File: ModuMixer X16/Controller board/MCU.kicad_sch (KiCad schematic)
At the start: 2 parts, among them U12 STM32F103RCTx

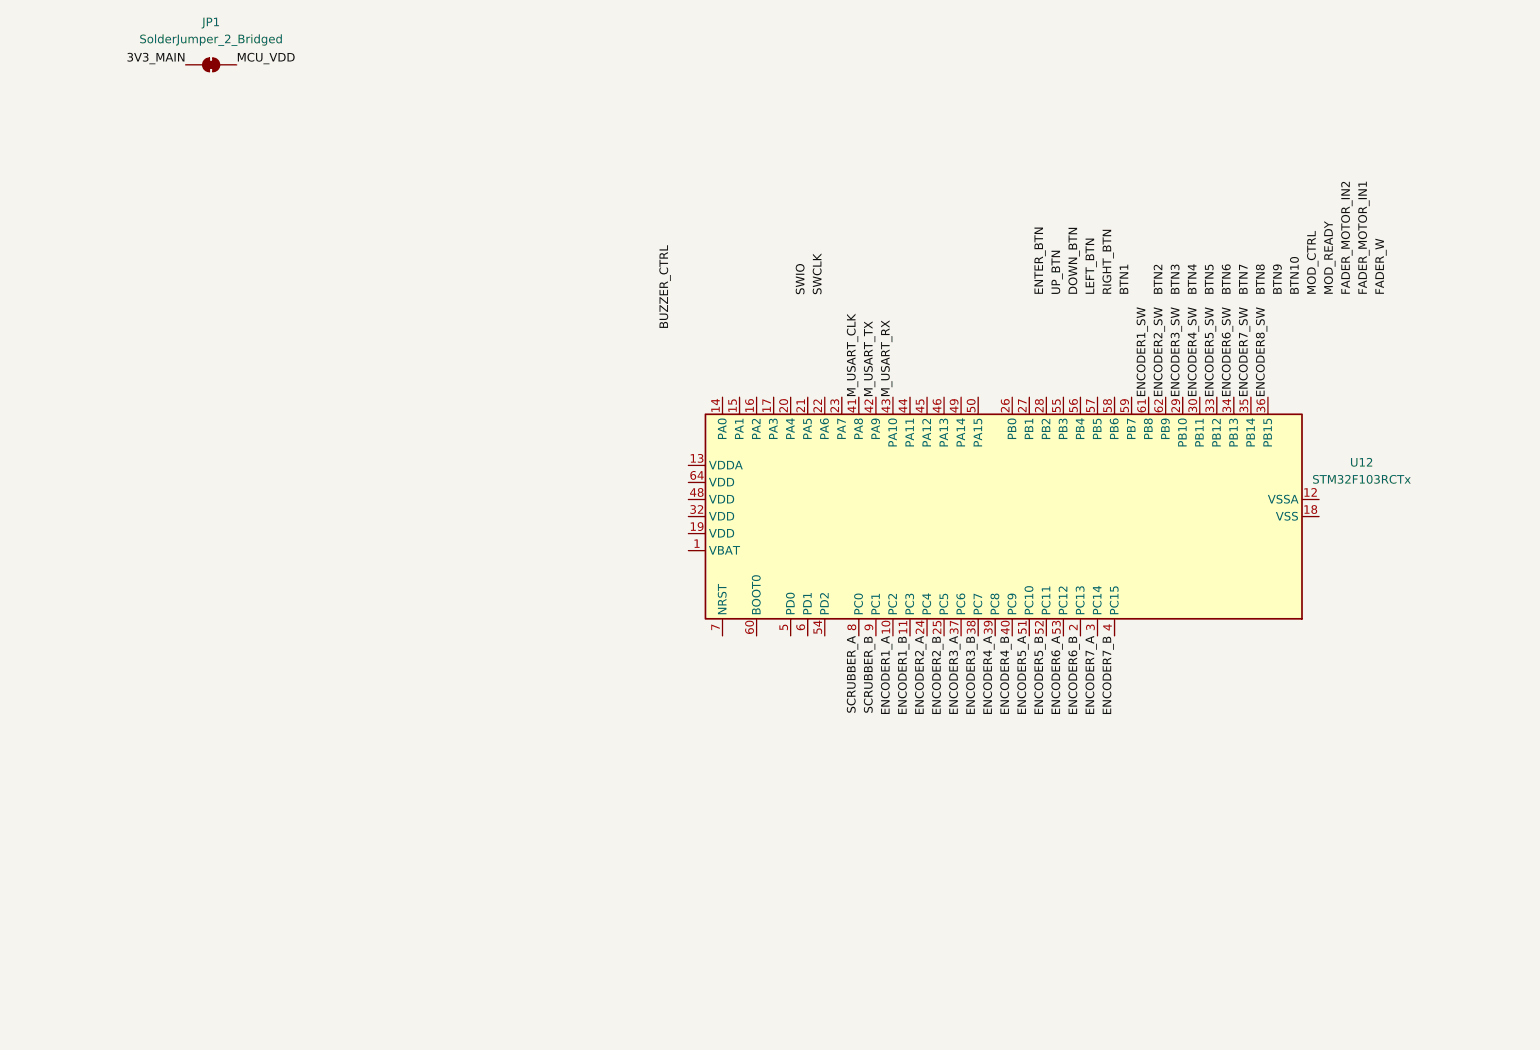
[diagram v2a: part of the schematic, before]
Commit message: Midway through MCU replacement
Sometimes i feel like it would be better to start over considering it's a digital mixer.
The only thing left is doing the DSP connections and calculating the values for a 16mhz crystal on all 3 MCUs
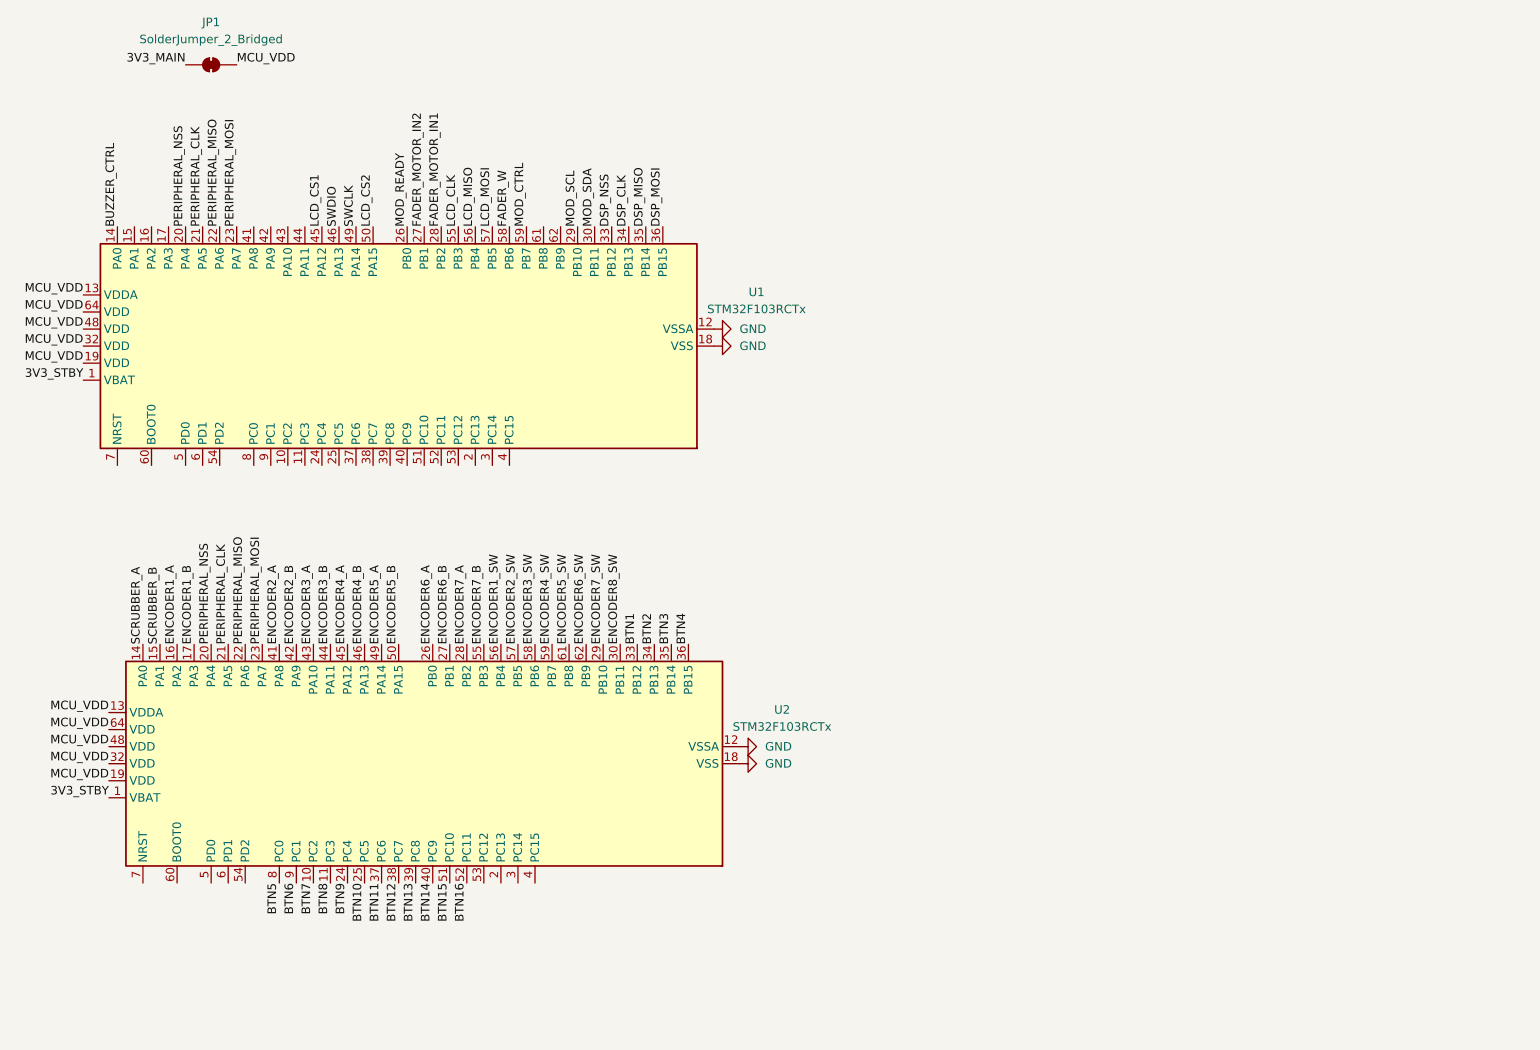
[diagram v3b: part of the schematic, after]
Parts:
- added U2: STM32F103RCTx, Package_QFP:LQFP-64_10x10mm_P0.5mm, symbol MCU_ST_STM32F1:STM32F103RCTx
- renumbered U12 to U1
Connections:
- net BTN1: now also U2.33 (PB12)
- net BTN10: now also U2.25 (PC5)
- net BTN2: now also U2.34 (PB13)
- net BTN3: now also U2.35 (PB14)
- net BTN4: now also U2.36 (PB15)
- net BTN5: now also U2.8 (PC0)
- net BTN6: now also U2.9 (PC1)
- net BTN7: now also U2.10 (PC2)
- net BTN8: now also U2.11 (PC3)
- net BTN9: now also U2.24 (PC4)
- net BUZZER_CTRL: now also U1.14 (PA0)
- net ENCODER1_A: now also U2.16 (PA2); no longer U1.10 (PC2)
- net ENCODER1_B: now also U2.17 (PA3); no longer U1.11 (PC3)
- net ENCODER1_SW: now also U2.56 (PB4); no longer U1.61 (PB8)
- net ENCODER2_A: now also U2.41 (PA8); no longer U1.24 (PC4)
- net ENCODER2_B: now also U2.42 (PA9); no longer U1.25 (PC5)
- net ENCODER2_SW: now also U2.57 (PB5); no longer U1.62 (PB9)
- net ENCODER3_A: now also U2.43 (PA10); no longer U1.37 (PC6)
- net ENCODER3_B: now also U2.44 (PA11); no longer U1.38 (PC7)
- net ENCODER3_SW: now also U2.58 (PB6); no longer U1.29 (PB10)
- net ENCODER4_A: now also U2.45 (PA12); no longer U1.39 (PC8)
- net ENCODER4_B: now also U2.46 (PA13); no longer U1.40 (PC9)
- net ENCODER4_SW: now also U2.59 (PB7); no longer U1.30 (PB11)
- net ENCODER5_A: now also U2.49 (PA14); no longer U1.51 (PC10)
- net ENCODER5_B: now also U2.50 (PA15); no longer U1.52 (PC11)
- net ENCODER5_SW: now also U2.61 (PB8); no longer U1.33 (PB12)
- net ENCODER6_A: now also U2.26 (PB0); no longer U1.53 (PC12)
- net ENCODER6_B: now also U2.27 (PB1); no longer U1.2 (PC13)
- net ENCODER6_SW: now also U2.62 (PB9); no longer U1.34 (PB13)
- net ENCODER7_A: now also U2.28 (PB2); no longer U1.3 (PC14)
- net ENCODER7_B: now also U2.55 (PB3); no longer U1.4 (PC15)
- net ENCODER7_SW: now also U2.29 (PB10); no longer U1.35 (PB14)
- net ENCODER8_SW: now also U2.30 (PB11); no longer U1.36 (PB15)
- net FADER_MOTOR_IN1: now also U1.28 (PB2)
- net FADER_MOTOR_IN2: now also U1.27 (PB1)
- net FADER_W: now also U1.58 (PB6)
- net MCU_VDD: now also U1.13 (VDDA), U1.19 (VDD), U1.32 (VDD), U1.48 (VDD), U1.64 (VDD), U2.13 (VDDA), U2.19 (VDD), U2.32 (VDD), U2.48 (VDD), U2.64 (VDD)
- net MOD_CTRL: now also U1.59 (PB7)
- net MOD_READY: now also U1.26 (PB0)
- net SCRUBBER_A: now also U2.14 (PA0); no longer U1.8 (PC0)
- net SCRUBBER_B: now also U2.15 (PA1); no longer U1.9 (PC1)
- net SWCLK: now also U1.49 (PA14)
- net 3V3_STBY: now reaches U1.1 (VBAT)
- net 3V3_STBY: now also U2.1 (VBAT)
- net GND: now reaches U1.12 (VSSA)
- net GND: now also U1.18 (VSS), U1.31 (VSS), U1.47 (VSS), U1.63 (VSS), U2.12 (VSSA), U2.18 (VSS), U2.31 (VSS), U2.47 (VSS), U2.63 (VSS)
- net PERIPHERAL_NSS: now reaches U1.20 (PA4)
- net PERIPHERAL_NSS: now also U2.20 (PA4)
- net PERIPHERAL_CLK: now reaches U1.21 (PA5)
- net PERIPHERAL_CLK: now also U2.21 (PA5)
- net PERIPHERAL_MISO: now reaches U1.22 (PA6)
- net PERIPHERAL_MISO: now also U2.22 (PA6)
- net PERIPHERAL_MOSI: now reaches U1.23 (PA7)
- net PERIPHERAL_MOSI: now also U2.23 (PA7)
- net LCD_CS1: now reaches U1.45 (PA12)
- net SWDIO: now reaches U1.46 (PA13)
- net LCD_CS2: now reaches U1.50 (PA15)
- net LCD_CLK: now reaches U1.55 (PB3)
- net LCD_MISO: now reaches U1.56 (PB4)
- net LCD_MOSI: now reaches U1.57 (PB5)
- net M_USART_CLK: no longer names the net of U1.41 (PA8)
- net M_USART_RX: no longer names the net of U1.43 (PA10)
- net M_USART_TX: no longer names the net of U1.42 (PA9)
- new net BTN11: U2.37 (PC6)
- new net BTN12: U2.38 (PC7)
- new net BTN13: U2.39 (PC8)
- new net BTN14: U2.40 (PC9)
- new net BTN15: U2.51 (PC10)
- new net BTN16: U2.52 (PC11)
- new net DSP_CLK: U1.34 (PB13)
- new net DSP_MISO: U1.35 (PB14)
- new net DSP_MOSI: U1.36 (PB15)
- new net DSP_NSS: U1.33 (PB12)
- new net MOD_SCL: U1.29 (PB10)
- new net MOD_SDA: U1.30 (PB11)
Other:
- moved on the sheet: U1

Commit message: MCU replacement done
I finally did everything (i guess), i replaced the MCUs, set the clock components, connected them, idk i guess it's ok now, we just gotta make that pcb
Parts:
- added C43, C44, C47, C48: 30pF, symbol Device:C
- added C45, C46: 20pF, symbol Device:C
- added C51, C52, C53, C54, C57, C58, C59, C60: 100nF, symbol Device:C
- added C55, C56: 1uF, symbol Device:C
- added JP7: SolderJumper_2_Bridged, Jumper:SolderJumper-2_P1.3mm_Bridged2Bar_Pad1.0x1.5mm, symbol Jumper:SolderJumper_2_Bridged
- added R20, R21, R8: 1M, symbol Device:R
- added Y1, Y3: 16MHz, Crystal:Crystal_HC49-U_Vertical, symbol Device:Crystal
- added Y2: 32.768KHz, Crystal:Crystal_HC49-U_Vertical, symbol Device:Crystal
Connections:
- net 3V3_MAIN: now also JP7.1 (A)
- net BTN1: now also U2.35 (PB14); no longer U2.33 (PB12)
- net BTN10: now also U2.38 (PC7); no longer U2.25 (PC5)
- net BTN11: now also U2.39 (PC8); no longer U2.37 (PC6)
- net BTN12: now also U2.40 (PC9); no longer U2.38 (PC7)
- net BTN13: now also U2.51 (PC10); no longer U2.39 (PC8)
- net BTN14: now also U2.52 (PC11); no longer U2.40 (PC9)
- net BTN15: now also U2.53 (PC12); no longer U2.51 (PC10)
- net BTN16: now also U2.2 (PC13); no longer U2.52 (PC11)
- net BTN2: now also U2.36 (PB15); no longer U2.34 (PB13)
- net BTN3: now also U2.8 (PC0); no longer U2.35 (PB14)
- net BTN4: now also U2.9 (PC1); no longer U2.36 (PB15)
- net BTN5: now also U2.10 (PC2); no longer U2.8 (PC0)
- net BTN6: now also U2.11 (PC3); no longer U2.9 (PC1)
- net BTN7: now also U2.24 (PC4); no longer U2.10 (PC2)
- net BTN8: now also U2.25 (PC5); no longer U2.11 (PC3)
- net BTN9: now also U2.37 (PC6); no longer U2.24 (PC4)
- net ENCODER1_SW: now also U2.58 (PB6); no longer U2.56 (PB4)
- net ENCODER2_SW: now also U2.59 (PB7); no longer U2.57 (PB5)
- net ENCODER3_SW: now also U2.61 (PB8); no longer U2.58 (PB6)
- net ENCODER4_B: now also U2.50 (PA15); no longer U2.46 (PA13)
- net ENCODER4_SW: now also U2.62 (PB9); no longer U2.59 (PB7)
- net ENCODER5_A: now also U2.26 (PB0); no longer U2.49 (PA14)
- net ENCODER5_B: now also U2.27 (PB1); no longer U2.50 (PA15)
- net ENCODER5_SW: now also U2.29 (PB10); no longer U2.61 (PB8)
- net ENCODER6_A: now also U2.28 (PB2); no longer U2.26 (PB0)
- net ENCODER6_B: now also U2.55 (PB3); no longer U2.27 (PB1)
- net ENCODER6_SW: now also U2.30 (PB11); no longer U2.62 (PB9)
- net ENCODER7_A: now also U2.56 (PB4); no longer U2.28 (PB2)
- net ENCODER7_B: now also U2.57 (PB5); no longer U2.55 (PB3)
- net ENCODER7_SW: now also U2.33 (PB12); no longer U2.29 (PB10)
- net ENCODER8_SW: now also U2.34 (PB13); no longer U2.30 (PB11)
- net GND: now also C43.2, C44.2, C45.2, C46.2, C47.2, C48.2, C51.2, C52.2, C53.2, C54.2, C55.1, C56.1, C57.2, C58.2, C59.2, C60.2
- net MCU_VDD: now also C51.1, C52.1, C53.1, C54.1, C55.2
- net PERIPHERAL_CLK1: now reaches U2.5 (PD0)
- net PERIPHERAL_CLK1: now also C47.1, R21.1, Y3.2
- net PERIPHERAL_CLK2: now reaches U2.6 (PD1)
- net PERIPHERAL_CLK2: now also C48.1, R21.2, Y3.1
- net PERIPHERAL_BOOT: now reaches U2.60 (BOOT0)
- net PERIPHERAL_RESET: now reaches U2.7 (NRST)
- net MAIN_RTC1: now reaches U1.3 (PC14)
- net MAIN_RTC1: now also C45.1, R20.1, Y2.2
- net MAIN_RTC2: now reaches U1.4 (PC15)
- net MAIN_RTC2: now also C46.1, R20.2, Y2.1
- net MAIN_CLK1: now reaches U1.5 (PD0)
- net MAIN_CLK1: now also C43.1, R8.1, Y1.2
- net MAIN_CLK2: now reaches U1.6 (PD1)
- net MAIN_CLK2: now also C44.1, R8.2, Y1.1
- net MAIN_BOOT: now reaches U1.60 (BOOT0)
- net MAIN_RESET: now reaches U1.7 (NRST)
- net SWCLK renamed MAIN_SWDCLK
- net SWDIO renamed MAIN_SWDIO
- new net PERIPHERAL_SWDCLK: U2.49 (PA14)
- new net PERIPHERAL_SWDIO: U2.46 (PA13)
- new net PERIPHERAL_VDD: C56.2, C57.1, C58.1, C59.1, C60.1, JP7.2 (B)
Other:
- moved on the sheet: JP1, U2

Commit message: asdasgashg
sfjhadgdjasdg
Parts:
- C1: renamed from C43; footprint (none) -> Capacitor_SMD:C_0603_1608Metric
- C10: renamed from C53; footprint (none) -> Capacitor_SMD:C_0603_1608Metric
- C11: renamed from C57; footprint (none) -> Capacitor_SMD:C_0603_1608Metric
- C12: renamed from C58; footprint (none) -> Capacitor_SMD:C_0603_1608Metric
- C13: renamed from C51; footprint (none) -> Capacitor_SMD:C_0603_1608Metric
- C14: renamed from C54; footprint (none) -> Capacitor_SMD:C_0603_1608Metric
- C15: renamed from C59; footprint (none) -> Capacitor_SMD:C_0603_1608Metric
- C16: renamed from C60; footprint (none) -> Capacitor_SMD:C_0603_1608Metric
- C2: renamed from C44; footprint (none) -> Capacitor_SMD:C_0603_1608Metric
- C3: renamed from C45; footprint (none) -> Capacitor_SMD:C_0603_1608Metric
- C4: renamed from C46; footprint (none) -> Capacitor_SMD:C_0603_1608Metric
- C5: renamed from C47; footprint (none) -> Capacitor_SMD:C_0603_1608Metric
- C6: renamed from C48; footprint (none) -> Capacitor_SMD:C_0603_1608Metric
- C7: renamed from C55; footprint (none) -> Capacitor_SMD:C_0603_1608Metric
- C8: renamed from C56; footprint (none) -> Capacitor_SMD:C_0603_1608Metric
- C9: renamed from C52; footprint (none) -> Capacitor_SMD:C_0603_1608Metric
- R1: renamed from R8; footprint (none) -> Resistor_SMD:R_0603_1608Metric
- R2: renamed from R20; footprint (none) -> Resistor_SMD:R_0603_1608Metric
- R3: renamed from R21; footprint (none) -> Resistor_SMD:R_0603_1608Metric
- renumbered JP7 to JP2
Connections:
- net BTN1: now also U2.8 (PC0); no longer U2.35 (PB14)
- net BTN10: now also U2.40 (PC9); no longer U2.38 (PC7)
- net BTN11: now also U2.51 (PC10); no longer U2.39 (PC8)
- net BTN12: now also U2.52 (PC11); no longer U2.40 (PC9)
- net BTN13: now also U2.53 (PC12); no longer U2.51 (PC10)
- net BTN14: now also U2.2 (PC13); no longer U2.52 (PC11)
- net BTN15: now also U2.3 (PC14); no longer U2.53 (PC12)
- net BTN16: now also U2.4 (PC15); no longer U2.2 (PC13)
- net BTN2: now also U2.9 (PC1); no longer U2.36 (PB15)
- net BTN3: now also U2.10 (PC2); no longer U2.8 (PC0)
- net BTN4: now also U2.11 (PC3); no longer U2.9 (PC1)
- net BTN5: now also U2.24 (PC4); no longer U2.10 (PC2)
- net BTN6: now also U2.25 (PC5); no longer U2.11 (PC3)
- net BTN7: now also U2.37 (PC6); no longer U2.24 (PC4)
- net BTN8: now also U2.38 (PC7); no longer U2.25 (PC5)
- net BTN9: now also U2.39 (PC8); no longer U2.37 (PC6)
- net ENCODER1_SW: now also U2.61 (PB8); no longer U2.58 (PB6)
- net ENCODER2_SW: now also U2.62 (PB9); no longer U2.59 (PB7)
- net ENCODER3_SW: now also U2.29 (PB10); no longer U2.61 (PB8)
- net ENCODER4_SW: now also U2.30 (PB11); no longer U2.62 (PB9)
- net ENCODER5_SW: now also U2.33 (PB12); no longer U2.29 (PB10)
- net ENCODER6_SW: now also U2.34 (PB13); no longer U2.30 (PB11)
- net ENCODER7_SW: now also U2.35 (PB14); no longer U2.33 (PB12)
- net ENCODER8_SW: now also U2.36 (PB15); no longer U2.34 (PB13)
- new net ENCODER8_A: U2.58 (PB6)
- new net ENCODER8_B: U2.59 (PB7)

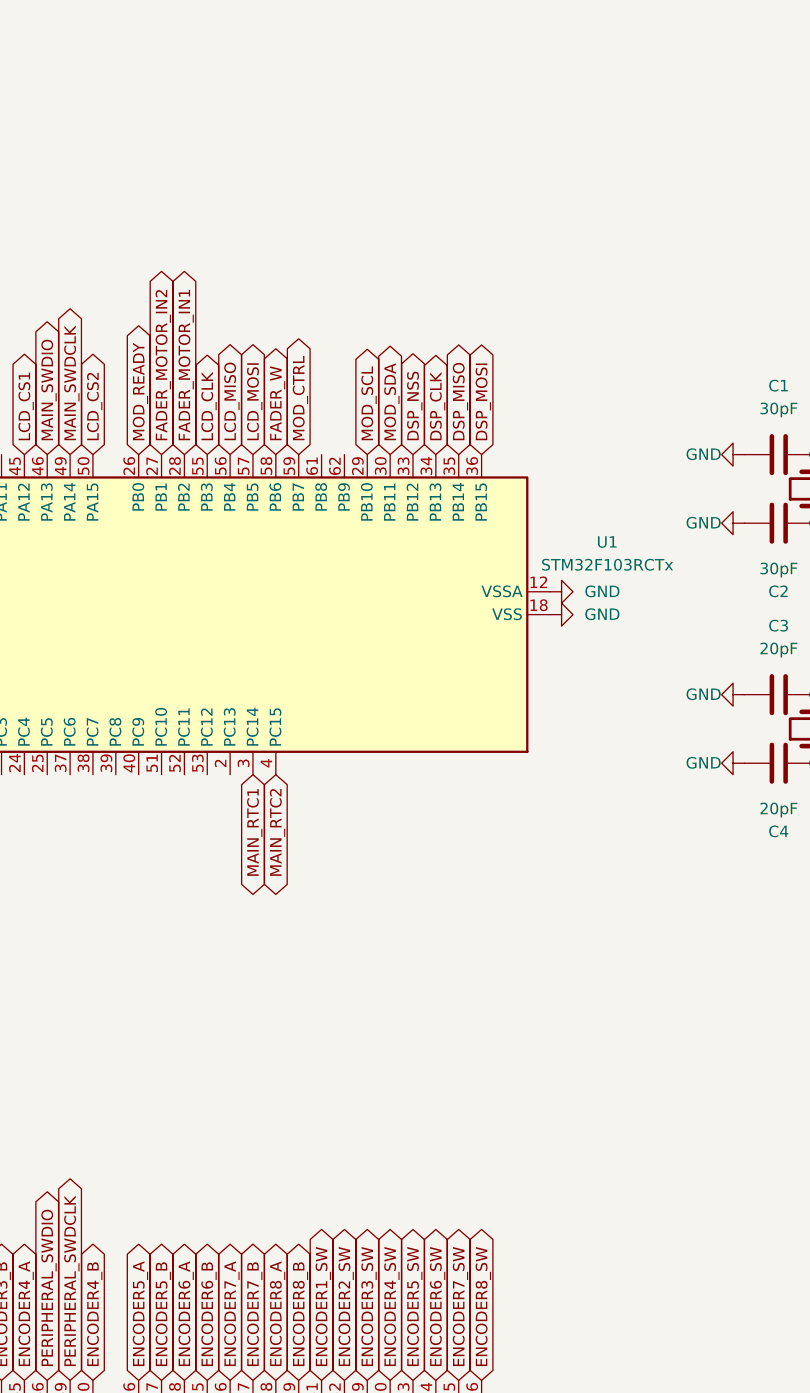
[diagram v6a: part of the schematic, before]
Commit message: MCU replacement finished
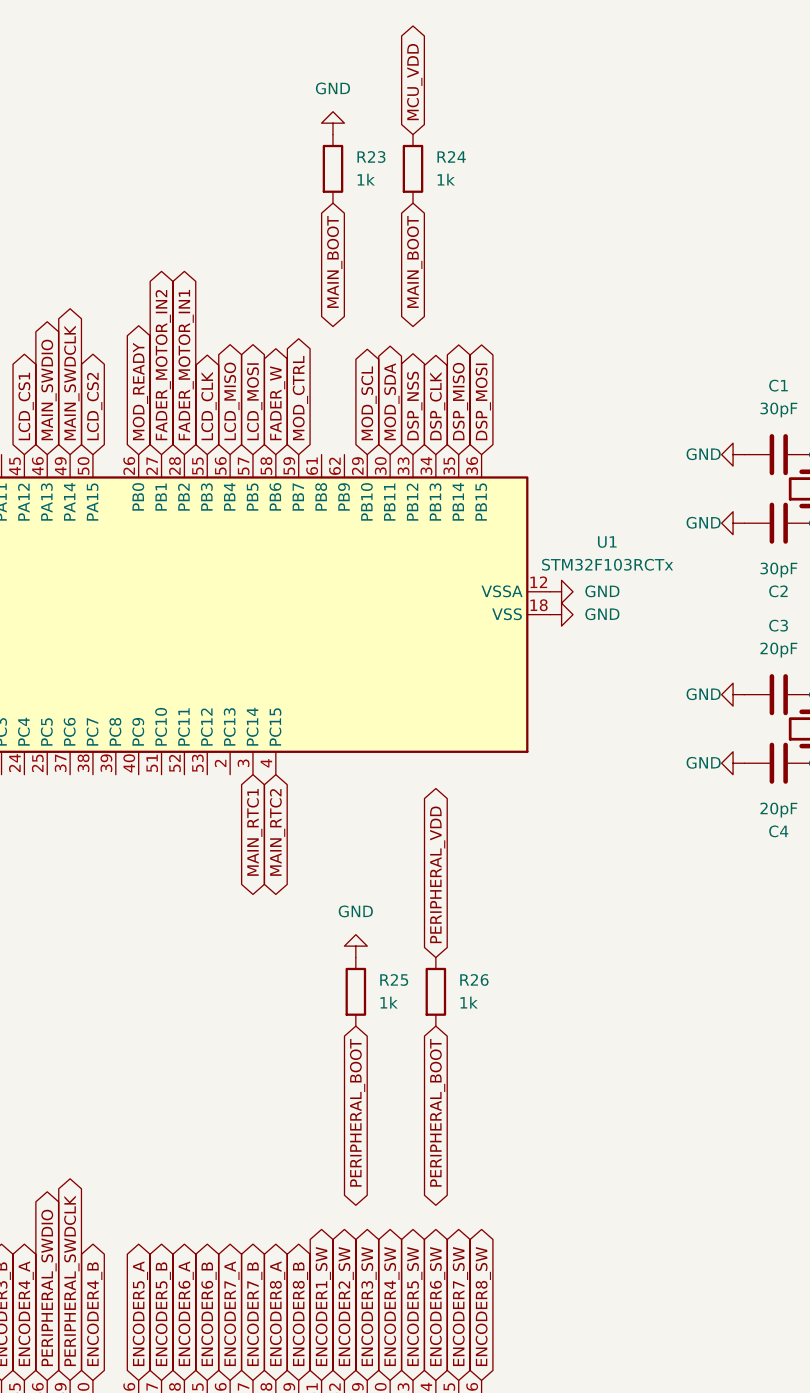
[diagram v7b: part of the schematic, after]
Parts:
- added R23, R24, R25, R26: 1k, Resistor_SMD:R_0603_1608Metric, symbol Device:R
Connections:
- net GND: now also R23.1, R25.1
- net MAIN_BOOT: now also R23.2, R24.2
- net MCU_VDD: now also R24.1
- net PERIPHERAL_BOOT: now also R25.2, R26.2
- net PERIPHERAL_VDD: now also R26.1
